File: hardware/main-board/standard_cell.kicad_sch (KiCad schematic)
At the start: 13 parts, among them J5 Conn_01x02_Pin, U10 TL071, U11 MT8816AF1, U12 MT8816AF1, U7 TL071, U8 AD5263BRUZ200, U9 AD5263BRUZ200

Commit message: Fully filled footprints
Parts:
- J5: footprint (none) -> Connector_PinHeader_1.00mm:PinHeader_1x02_P1.00mm_Horizontal
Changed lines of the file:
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@@
 			)
 		)
-		(property "Footprint" ""
+		(property "Footprint" "Connector_PinHeader_1.00mm:PinHeader_1x02_P1.00mm_Horizontal"
 			(at 238.76 33.02 0)
 			(effects

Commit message: PCB comps in, and formatted
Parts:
- U11, U12: footprint MT8816AF1:QFP80P1200X1200X120-44N -> SeniorDesignFP:QFP80P1200X1200X120-44N
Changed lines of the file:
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@@
 			)
 		)
-		(property "Footprint" "MT8816AF1:QFP80P1200X1200X120-44N"
+		(property "Footprint" "SeniorDesignFP:QFP80P1200X1200X120-44N"
 			(at 140.716 172.212 0)
 			(effects
@@
 			)
 		)
-		(property "Footprint" "MT8816AF1:QFP80P1200X1200X120-44N"
+		(property "Footprint" "SeniorDesignFP:QFP80P1200X1200X120-44N"
 			(at 239.014 172.212 0)
 			(effects

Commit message: designed Power PCB section layout
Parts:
- removed U11, U12: MT8816AF1, SeniorDesignFP:QFP80P1200X1200X120-44N, symbol SeniorDesign:MT8816AF1
- added U11, U12: CD22M3494MQZ, SeniorDesignFP:PLCC44_16P66X16P66_INR-M, symbol SeniorDesign:CD22M3494MQZ
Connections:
- net C1_in: now also U11.31 (X0)
- net C1_out: now also U11.30 (X1)
- net C2_in: now also U11.29 (X2)
- net C2_out: now also U11.28 (X3)
- net C3_in: now also U11.27 (X4)
- net C3_out: now also U11.26 (X5)
- net C4_in: now also U11.6 (X8)
- net C4_out: now also U11.7 (X9)
- net D1_anode: now also U11.5 (X7)
- net D1_cathode: now also U11.4 (X6)
- net D2_anode: now also U11.24 (X13)
- net D2_cathode: now also U11.25 (X12)
- net GND: now also U11.15 (Y5), U12.15 (Y5)
- net Input_1: now also U11.32 (Y0), U12.32 (Y0)
- net Input_2: now also U11.35 (Y1), U12.35 (Y1)
- net Input_3: now also U11.37 (Y2), U12.37 (Y2)
- net J1_in: now also U11.2 (X14)
- net J1_out: now also U11.3 (X15)
- net Op1_neg: now also U12.29 (X2)
- net Op1_out: now also U12.31 (X0)
- net Op1_pos: now also U12.30 (X1)
- net Op2_neg: now also U12.26 (X5)
- net Op2_out: now also U12.28 (X3)
- net Op2_pos: now also U12.27 (X4)
- net Output: now also U11.39 (Y3), U12.39 (Y3)
- net R1_in: now also U12.25 (X12)
- net R1_out: now also U12.24 (X13)
- net R2_in: now also U12.2 (X14)
- net R2_out: now also U12.3 (X15)
- net R3_in: now also U12.4 (X6)
- net R3_out: now also U12.5 (X7)
- net R4_in: now also U12.6 (X8)
- net R4_out: now also U12.7 (X9)
- net R5_in: now also U12.8 (X10)
- net R5_out: now also U12.9 (X11)
- net R6_in: now also U11.8 (X10)
- net R6_out: now also U11.9 (X11)
- new net: U11.10 (Y7), U12.10 (Y7)
- new net: U11.13 (Y6), U12.13 (Y6)
- new net: U11.17 (Y4), U12.17 (Y4)
- no-connect marks 0 -> 10

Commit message: Working on that PCP
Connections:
- net C1_in: now also U12.25 (X12); no longer U11.31 (X0)
- net C1_out: now also U12.24 (X13); no longer U11.30 (X1)
- net C2_in: now also U11.8 (X10); no longer U11.29 (X2)
- net C2_out: now also U11.9 (X11); no longer U11.28 (X3)
- net J1_in: now also J5.2 (Pin_2); no longer J5.1 (Pin_1)
- net J1_out: now also J5.1 (Pin_1); no longer J5.2 (Pin_2)
- net Op1_neg: now also U12.30 (X1); no longer U12.29 (X2)
- net Op1_pos: now also U12.29 (X2); no longer U12.30 (X1)
- net Op2_neg: now also U12.27 (X4); no longer U12.26 (X5)
- net Op2_pos: now also U12.26 (X5); no longer U12.27 (X4)
- net R1_in: now also U12.4 (X6); no longer U12.25 (X12)
- net R1_out: now also U12.5 (X7); no longer U12.24 (X13)
- net R2_in: now also U12.6 (X8); no longer U12.2 (X14)
- net R2_out: now also U12.7 (X9); no longer U12.3 (X15)
- net R3_in: now also U12.2 (X14); no longer U12.4 (X6)
- net R3_out: now also U12.3 (X15); no longer U12.5 (X7)
- net R4_in: now also U12.8 (X10); no longer U12.6 (X8)
- net R4_out: now also U12.9 (X11); no longer U12.7 (X9)
- net R5_in: now also U11.31 (X0); no longer U12.8 (X10)
- net R5_out: now also U11.30 (X1); no longer U12.9 (X11)
- net R6_in: now also U11.29 (X2), U9.4 (B3); no longer U11.8 (X10), U9.24 (B2)
- net R6_out: now also U11.28 (X3), U9.5 (A3), U9.6 (W3); no longer U11.9 (X11), U9.22 (W2), U9.23 (A2)
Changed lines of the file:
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@@
 		(color 0 0 0 0)
+	)
+	(junction
+		(at 50.8 162.56)
+		(diameter 0)
+		(color 0 0 0 0)
+	)
+	(no_connect
+		(at 81.28 146.05)
+	)
+	(no_connect
+		(at 81.28 120.65)
 	)
 	(no_connect
@@
 	)
 	(no_connect
-		(at 39.37 175.26)
+		(at 81.28 175.26)
 	)
 	(no_connect
-		(at 81.28 175.26)
-	)
-	(no_connect
-		(at 39.37 149.86)
-	)
-	(no_connect
-		(at 50.8 162.56)
+		(at 92.71 133.35)
 	)
 	(no_connect
@@
 	(wire
 		(pts
+			(xy 50.8 162.56) (xy 50.8 149.86)
+		)
+		(stroke
+			(width 0)
+			(type default)
+		)
+	)
+	(wire
+		(pts
+			(xy 251.46 33.02) (xy 243.84 33.02)
+		)
+		(stroke
+			(width 0)
+			(type default)
+		)
+	)
+	(wire
+		(pts
 			(xy 180.34 118.11) (xy 182.88 118.11)
 		)
@@
 	(wire
 		(pts
-			(xy 92.71 120.65) (xy 81.28 120.65)
-		)
-		(stroke
-			(width 0)
-			(type default)
-		)
-	)
-	(wire
-		(pts
 			(xy 190.5 96.52) (xy 190.5 110.49)
 		)
@@
 	(wire
 		(pts
+			(xy 50.8 162.56) (xy 53.34 162.56)
+		)
+		(stroke
+			(width 0)
+			(type default)
+		)
+	)
+	(wire
+		(pts
 			(xy 186.69 123.19) (xy 199.39 123.19)
 		)
@@
 	(wire
 		(pts
-			(xy 92.71 133.35) (xy 93.98 133.35)
-		)
-		(stroke
-			(width 0)
-			(type default)
-		)
-	)
-	(wire
-		(pts
 			(xy 92.71 104.14) (xy 92.71 91.44)
 		)
@@
 	(wire
 		(pts
-			(xy 243.84 33.02) (xy 252.73 33.02)
-		)
-		(stroke
-			(width 0)
-			(type default)
-		)
-	)
-	(wire
-		(pts
 			(xy 182.88 118.11) (xy 182.88 138.43)
 		)
@@
 	(wire
 		(pts
+			(xy 39.37 176.53) (xy 39.37 175.26)
+		)
+		(stroke
+			(width 0)
+			(type default)
+		)
+	)
+	(wire
+		(pts
 			(xy 50.8 104.14) (xy 50.8 91.44)
 		)
@@
 	(wire
 		(pts
+			(xy 251.46 35.56) (xy 243.84 35.56)
+		)
+		(stroke
+			(width 0)
+			(type default)
+		)
+	)
+	(wire
+		(pts
 			(xy 92.71 91.44) (xy 81.28 91.44)
 		)
@@
 	(wire
 		(pts
+			(xy 50.8 149.86) (xy 39.37 149.86)
+		)
+		(stroke
+			(width 0)
+			(type default)
+		)
+	)
+	(wire
+		(pts
 			(xy 182.88 118.11) (xy 199.39 118.11)
 		)
@@
 		(pts
 			(xy 50.8 133.35) (xy 50.8 120.65)
-		)
-		(stroke
-			(width 0)
-			(type default)
-		)
-	)
-	(wire
-		(pts
-			(xy 92.71 133.35) (xy 92.71 120.65)
-		)
-		(stroke
-			(width 0)
-			(type default)
-		)
-	)
-	(wire
-		(pts
-			(xy 243.84 35.56) (xy 252.73 35.56)
 		)
 		(stroke
@@
 	)
 	(label "R2_in"
-		(at 234.95 144.78 0)
+		(at 234.95 129.54 0)
 		(effects
 			(font
@@
 	)
 	(label "R6_in"
-		(at 81.28 146.05 0)
+		(at 39.37 176.53 0)
 		(effects
 			(font
@@
 	)
 	(label "C2_in"
-		(at 144.78 114.3 180)
+		(at 144.78 134.62 180)
 		(effects
 			(font
@@
 	)
 	(label "R3_out"
-		(at 234.95 127 0)
+		(at 234.95 147.32 0)
 		(effects
 			(font
@@
 	)
 	(label "C2_out"
-		(at 144.78 116.84 180)
+		(at 144.78 137.16 180)
 		(effects
 			(font
@@
 	)
 	(label "Op2_neg"
-		(at 234.95 121.92 0)
+		(at 234.95 119.38 0)
 		(effects
 			(font
@@
 	)
 	(label "C1_out"
-		(at 144.78 111.76 180)
-		(effects
-			(font
-				(size 1.016 1.016)
-			)
-			(justify right)
+		(at 234.95 142.24 0)
+		(effects
+			(font
+				(size 1.016 1.016)
+			)
+			(justify left)
 		)
 	)
@@
 	)
 	(label "J1_out"
-		(at 252.73 35.56 0)
+		(at 251.46 33.02 0)
 		(effects
 			(font
@@
 	)
 	(label "C1_in"
-		(at 144.78 109.22 180)
-		(effects
-			(font
-				(size 1.016 1.016)
-			)
-			(justify right)
+		(at 234.95 139.7 0)
+		(effects
+			(font
+				(size 1.016 1.016)
+			)
+			(justify left)
 		)
 	)
 	(label "R5_out"
-		(at 234.95 137.16 0)
-		(effects
-			(font
-				(size 1.016 1.016)
-			)
-			(justify left)
+		(at 144.78 111.76 180)
+		(effects
+			(font
+				(size 1.016 1.016)
+			)
+			(justify right)
 		)
 	)
@@
 	)
 	(label "Op2_pos"
-		(at 234.95 119.38 0)
+		(at 234.95 121.92 0)
 		(effects
 			(font
@@
 	)
 	(label "R2_out"
-		(at 234.95 147.32 0)
+		(at 234.95 132.08 0)
 		(effects
 			(font
@@
 	)
 	(label "R6_out"
-		(at 93.98 133.35 0)
+		(at 53.34 162.56 0)
 		(effects
 			(font
@@
 	)
 	(label "R6_in"
-		(at 144.78 134.62 180)
+		(at 144.78 114.3 180)
 		(effects
 			(font
@@
 	)
 	(label "R6_out"
-		(at 144.78 137.16 180)
+		(at 144.78 116.84 180)
 		(effects
 			(font
@@
 	)
 	(label "R4_out"
-		(at 234.95 132.08 0)
+		(at 234.95 137.16 0)
 		(effects
 			(font
@@
 	)
 	(label "Op1_pos"
-		(at 234.95 111.76 0)
+		(at 234.95 114.3 0)
 		(effects
 			(font
@@
 	)
 	(label "R4_in"
-		(at 234.95 129.54 0)
+		(at 234.95 134.62 0)
 		(effects
 			(font
@@
 	)
 	(label "R1_out"
-		(at 234.95 142.24 0)
+		(at 234.95 127 0)
 		(effects
 			(font
@@
 	)
 	(label "Op1_neg"
-		(at 234.95 114.3 0)
+		(at 234.95 111.76 0)
 		(effects
 			(font
@@
 	)
 	(label "R1_in"
-		(at 234.95 139.7 0)
+		(at 234.95 124.46 0)
 		(effects
 			(font
@@
 	)
 	(label "R3_in"
-		(at 234.95 124.46 0)
+		(at 234.95 144.78 0)
 		(effects
 			(font
@@
 	)
 	(label "J1_in"
-		(at 252.73 33.02 0)
+		(at 251.46 35.56 0)
 		(effects
 			(font
@@
 	)
 	(label "R5_in"
-		(at 234.95 134.62 0)
-		(effects
-			(font
-				(size 1.016 1.016)
-			)
-			(justify left)
-		)
-	)
+		(at 144.78 109.22 180)
+		(effects
+			(font
+				(size 1.016 1.016)
+			)
+			(justify right)
+		)
+	)

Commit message: The PCB is coming together
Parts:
- J5: footprint Connector_PinHeader_1.00mm:PinHeader_1x02_P1.00mm_Horizontal -> Connector_PinSocket_2.54mm:PinSocket_1x02_P2.54mm_Vertical
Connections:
- net C2_in: now also U11.2 (X14); no longer U11.8 (X10)
- net C2_out: now also U11.3 (X15); no longer U11.9 (X11)
- net C3_in: now also U11.8 (X10); no longer U11.27 (X4)
- net C3_out: now also U11.9 (X11); no longer U11.26 (X5)
- net Input_1: now also U12.17 (Y4); no longer U12.32 (Y0)
- net Input_2: now also U12.15 (Y5); no longer U12.35 (Y1)
- net Input_3: now also U12.13 (Y6); no longer U12.37 (Y2)
- net J1_in: now also U11.27 (X4); no longer U11.2 (X14)
- net J1_out: now also U11.26 (X5); no longer U11.3 (X15)
- net Op1_neg: now also U12.29 (X2); no longer U12.30 (X1)
- net Op1_pos: now also U12.30 (X1); no longer U12.29 (X2)
- net Output: now also U12.10 (Y7); no longer U12.39 (Y3)
- net R1_in: now also U12.5 (X7); no longer U12.4 (X6)
- net R1_out: now also U12.4 (X6); no longer U12.5 (X7)
- net R3_in: now also U12.3 (X15); no longer U12.2 (X14)
- net R3_out: now also U12.2 (X14); no longer U12.3 (X15)
- net Y7: now reaches U11.10 (Y7)
- net Y7: now also U12.39 (Y3); no longer U12.10 (Y7)
- net Y6: now reaches U11.13 (Y6)
- net Y6: now also U12.37 (Y2); no longer U12.13 (Y6)
- net Y4: now reaches U11.17 (Y4)
- net Y4: now also U12.32 (Y0); no longer U12.17 (Y4)
- net GND renamed Y5
- net Y5: now also U12.35 (Y1); no longer U12.15 (Y5)

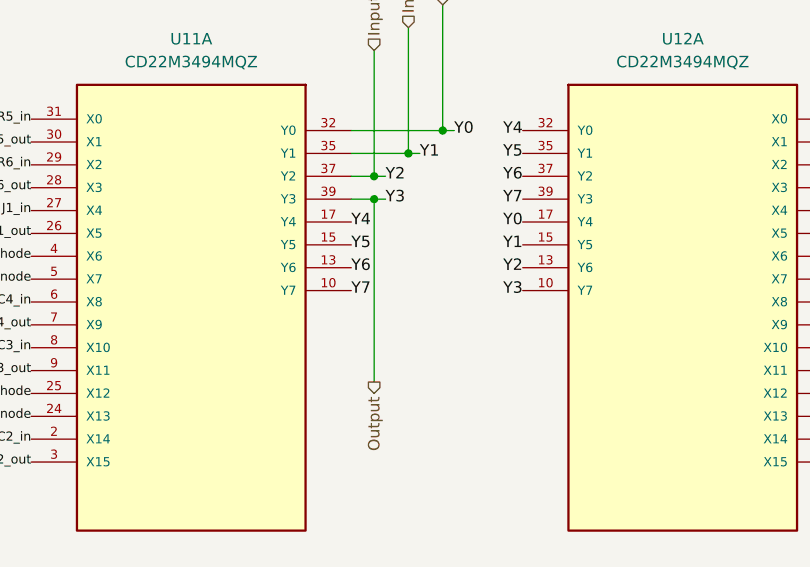
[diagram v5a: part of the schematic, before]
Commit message: feat: ERC + DRC fixes
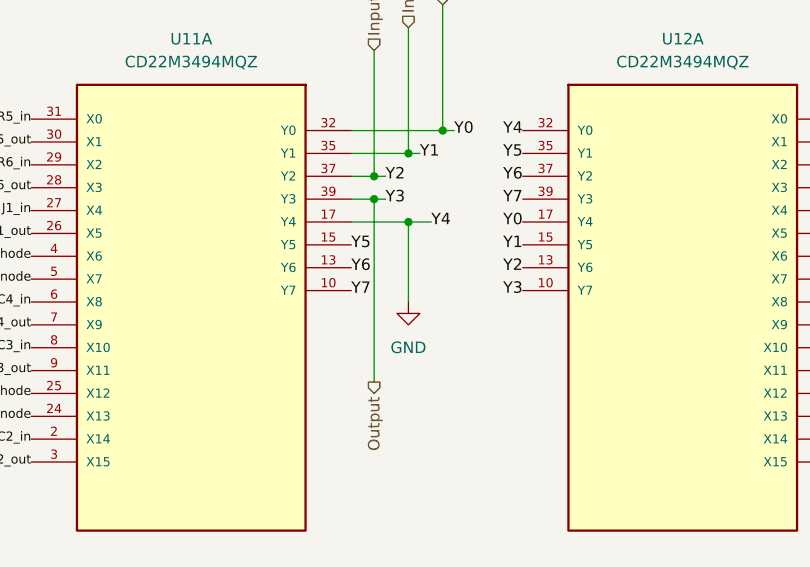
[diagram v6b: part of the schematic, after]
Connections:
- net Y4 renamed GND
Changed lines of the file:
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@@
+	)
+	(junction
+		(at 186.69 120.65)
+		(diameter 0)
+		(color 0 0 0 0)
 	)
 	(junction
@@
 	(wire
 		(pts
+			(xy 186.69 120.65) (xy 186.69 129.54)
+		)
+		(stroke
+			(width 0)
+			(type default)
+		)
+	)
+	(wire
+		(pts
 			(xy 50.8 133.35) (xy 52.07 133.35)
 		)
@@
 	(wire
 		(pts
+			(xy 186.69 120.65) (xy 180.34 120.65)
+		)
+		(stroke
+			(width 0)
+			(type default)
+		)
+	)
+	(wire
+		(pts
 			(xy 92.71 104.14) (xy 95.25 104.14)
 		)
@@
 	(wire
 		(pts
+			(xy 189.23 120.65) (xy 186.69 120.65)
+		)
+		(stroke
+			(width 0)
+			(type default)
+		)
+	)
+	(wire
+		(pts
 			(xy 50.8 133.35) (xy 50.8 120.65)
 		)
@@
 	)
 	(label "Y4"
-		(at 180.34 120.65 0)
+		(at 189.23 120.65 0)
 		(effects
 			(font
@@
 					(unit 1)
 				)
+			)
+		)
+	)
+	(symbol
+		(lib_id "power:GND")
+		(at 186.69 129.54 0)
+		(unit 1)
+		(exclude_from_sim no)
+		(in_bom yes)
+		(on_board yes)
+		(dnp no)
+		(fields_autoplaced yes)
+		(property "Reference" "#PWR0157"
+			(at 186.69 135.89 0)
+			(effects
+				(font
+					(size 1.27 1.27)
+				)
+				(hide yes)
+			)
+		)
+		(property "Value" "GND"
+			(at 186.69 134.62 0)
+			(effects
+				(font
+					(size 1.27 1.27)
+				)
+			)
+		)
+		(property "Footprint" ""
+			(at 186.69 129.54 0)
+			(effects
+				(font
+					(size 1.27 1.27)
+				)
+				(hide yes)
+			)
+		)
+		(property "Datasheet" ""
+			(at 186.69 129.54 0)
+			(effects
+				(font
+					(size 1.27 1.27)
+				)
+				(hide yes)
+			)
+		)
+		(property "Description" "Power symbol creates a global label with name \"GND\" , ground"
+			(at 186.69 129.54 0)
+			(effects
+				(font
+					(size 1.27 1.27)
+				)
+				(hide yes)
+			)
+		)
+		(pin "1"
+		)
+		(instances
+			(project ""
+				(path "/5dd933ff-bc57-4741-8957-85d8c6e75130/1dabda79-d399-4710-9868-c914be4636dc"
+					(reference "#PWR0159")
+					(unit 1)
+				)
+				(path "/5dd933ff-bc57-4741-8957-85d8c6e75130/976c758a-cbac-4a5f-b407-9f4ceba4ebf5"
+					(reference "#PWR0160")
+					(unit 1)
+				)
+				(path "/5dd933ff-bc57-4741-8957-85d8c6e75130/f2ad4040-6970-4225-8b08-e82169e71be0"
+					(reference "#PWR0158")
+					(unit 1)
+				)
+				(path "/5dd933ff-bc57-4741-8957-85d8c6e75130/fe3808c0-aea1-40d0-81b1-a52454b6fcf3"
+					(reference "#PWR0157")
+					(unit 1)
+				)

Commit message: feat: Diodes bigger
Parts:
- D1, D2: footprint Diode_SMD:D_SOD-523 -> Diode_SMD:D_SOD-123; DKPN (none) -> 1655-1N4148WCT-ND
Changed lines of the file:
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@@
 			)
 		)
-		(property "Footprint" "Diode_SMD:D_SOD-523"
+		(property "Footprint" "Diode_SMD:D_SOD-123"
 			(at 177.8 45.085 0)
 			(effects
@@
 		)
 		(property "Sim.Pins" "1=K 2=A"
+			(at 177.8 40.64 0)
+			(effects
+				(font
+					(size 1.27 1.27)
+				)
+				(hide yes)
+			)
+		)
+		(property "DKPN" "1655-1N4148WCT-ND"
 			(at 177.8 40.64 0)
 			(effects
@@
 			)
 		)
-		(property "Footprint" "Diode_SMD:D_SOD-523"
+		(property "Footprint" "Diode_SMD:D_SOD-123"
 			(at 177.8 32.385 0)
 			(effects
@@
 			(at 177.8 27.94 0)
 			(effects
+				(font
+					(size 1.27 1.27)
+				)
+				(hide yes)
+			)
+		)
+		(property "DKPN" "1655-1N4148WCT-ND"
+			(at 177.8 27.94 0)
+			(effects

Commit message: feat: Part nos plus some micro fixup
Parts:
- C1: DKPN (none) -> C0603C105K4RACTU
- C2: DKPN (none) -> C0603C104K5RACTU
- C3: DKPN (none) -> C0603C103K5RACTU
- C4: DKPN (none) -> C0603C102K5RACTU
- D1, D2: DKPN 1655-1N4148WCT-ND -> 1N4148W
- U10, U7: DKPN (none) -> TL071HIDR
- U11, U12: MPN (none) -> 968-CD22M3494MQZ
- U8, U9: DKPN (none) -> AD5263BRUZ200-R7; MPN AD5263BRUZ200 -> (none)
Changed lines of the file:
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@@
 			)
 		)
-		(property "MPN" "AD5263BRUZ200"
+		(property "MPN" ""
 			(at 165.354 229.108 0)
 			(effects
@@
 			)
 		)
+		(property "DKPN" "AD5263BRUZ200-R7"
+			(at 50.8 182.88 0)
+			(effects
+				(font
+					(size 1.27 1.27)
+				)
+				(hide yes)
+			)
+		)
 		(pin "10"
 		)
@@
 			)
 		)
-		(property "DKPN" "1655-1N4148WCT-ND"
+		(property "DKPN" "1N4148W"
 			(at 177.8 40.64 0)
 			(effects
@@
 			)
 		)
-		(property "MPN" "AD5263BRUZ200"
+		(property "MPN" ""
 			(at 166.624 140.208 0)
 			(effects
@@
 			)
 		)
+		(property "DKPN" "AD5263BRUZ200-R7"
+			(at 52.07 93.98 0)
+			(effects
+				(font
+					(size 1.27 1.27)
+				)
+				(hide yes)
+			)
+		)
 		(pin "7"
 		)
@@
 			)
 		)
-		(property "MPN" "AD5263BRUZ200"
+		(property "MPN" ""
 			(at 166.624 199.898 0)
 			(effects
@@
 			)
 		)
+		(property "DKPN" "AD5263BRUZ200-R7"
+			(at 52.07 153.67 0)
+			(effects
+				(font
+					(size 1.27 1.27)
+				)
+				(hide yes)
+			)
+		)
 		(pin "10"
 		)
@@
 			)
 		)
+		(property "DKPN" "TL071HIDR"
+			(at 115.57 33.02 0)
+			(effects
+				(font
+					(size 1.27 1.27)
+				)
+				(hide yes)
+			)
+		)
 		(pin "5"
 		)
@@
 			)
 		)
+		(property "DKPN" "C0603C104K5RACTU"
+			(at 146.05 68.58 0)
+			(effects
+				(font
+					(size 1.27 1.27)
+				)
+				(hide yes)
+			)
+		)
 		(pin "1"
 		)
@@
 			)
 		)
-		(property "MPN" "AD5263BRUZ200"
+		(property "MPN" ""
 			(at 207.264 169.418 0)
 			(effects
@@
 			)
 		)
+		(property "DKPN" "AD5263BRUZ200-R7"
+			(at 92.71 123.19 0)
+			(effects
+				(font
+					(size 1.27 1.27)
+				)
+				(hide yes)
+			)
+		)
 		(pin "7"
 		)
@@
 			)
 		)
-		(property "MPN" "AD5263BRUZ200"
+		(property "MPN" ""
 			(at 207.264 140.208 0)
 			(effects
@@
 			)
 		)
+		(property "DKPN" "AD5263BRUZ200-R7"
+			(at 92.71 93.98 0)
+			(effects
+				(font
+					(size 1.27 1.27)
+				)
+				(hide yes)
+			)
+		)
 		(pin "7"
 		)
@@
 			)
 		)
-		(property "MPN" "AD5263BRUZ200"
+		(property "MPN" ""
 			(at 207.264 199.898 0)
 			(effects
@@
 			)
 		)
+		(property "DKPN" "AD5263BRUZ200-R7"
+			(at 92.71 153.67 0)
+			(effects
+				(font
+					(size 1.27 1.27)
+				)
+				(hide yes)
+			)
+		)
 		(pin "10"
 		)
@@
 			)
 		)
+		(property "DKPN" "C0603C103K5RACTU"
+			(at 165.1 68.58 0)
+			(effects
+				(font
+					(size 1.27 1.27)
+				)
+				(hide yes)
+			)
+		)
 		(pin "2"
 		)
@@
 			)
 		)
-		(property "MPN" "AD5263BRUZ200"
+		(property "MPN" ""
 			(at 207.264 227.838 0)
 			(effects
@@
 			)
 		)
+		(property "DKPN" "AD5263BRUZ200-R7"
+			(at 92.71 181.61 0)
+			(effects
+				(font
+					(size 1.27 1.27)
+				)
+				(hide yes)
+			)
+		)
 		(pin "10"
 		)
@@
 			)
 		)
+		(property "DKPN" "C0603C102K5RACTU"
+			(at 185.42 68.58 0)
+			(effects
+				(font
+					(size 1.27 1.27)
+				)
+				(hide yes)
+			)
+		)
 		(pin "2"
 		)
@@
 			)
 		)
+		(property "MPN" "968-CD22M3494MQZ"
+			(at 162.56 146.05 0)
+			(effects
+				(font
+					(size 1.27 1.27)
+				)
+				(hide yes)
+			)
+		)
 		(pin "13"
 		)
@@
 			)
 		)
-		(property "MPN" "AD5263BRUZ200"
+		(property "MPN" ""
 			(at 165.354 170.688 0)
 			(effects
@@
 			)
 		)
+		(property "DKPN" "AD5263BRUZ200-R7"
+			(at 50.8 124.46 0)
+			(effects
+				(font
+					(size 1.27 1.27)
+				)
+				(hide yes)
+			)
+		)
 		(pin "7"
 		)
@@
 			)
 		)
+		(property "DKPN" "C0603C105K4RACTU"
+			(at 125.73 68.58 0)
+			(effects
+				(font
+					(size 1.27 1.27)
+				)
+				(hide yes)
+			)
+		)
 		(pin "1"
 		)
@@
 			)
 		)
-		(property "DKPN" "1655-1N4148WCT-ND"
+		(property "DKPN" "1N4148W"
 			(at 177.8 27.94 0)
 			(effects
@@
 			)
 		)
+		(property "MPN" "968-CD22M3494MQZ"
+			(at 217.17 146.05 0)
+			(effects
+				(font
+					(size 1.27 1.27)
+				)
+				(hide yes)
+			)
+		)
 		(pin "37"
 		)
@@
 			(at 50.8 33.02 0)
 			(effects
+				(font
+					(size 1.27 1.27)
+				)
+				(hide yes)
+			)
+		)
+		(property "DKPN" "TL071HIDR"
+			(at 50.8 33.02 0)
+			(effects
